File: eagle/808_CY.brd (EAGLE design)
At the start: 100 x 80 mm, 112 parts, among them IC1 TL071P, IC2 TL071P, IC3 TL071P, IC4 TL072P, Q1 2N3904, Q2 2N3904, Q3 2N3904, Q4 2N3904, Q5 2N3904, Q6 2N3904, Q7 2N3904, Q8 2N3906

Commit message: finishing routes manually
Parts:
- R105*: device TR808clone:0207/5V -> TR808clone:0309/10
- R126*: device TR808clone:0207/5V -> TR808clone:0207/7
- moved R126* 13.6 mm to (94.6, 52.1)
- moved R105* 8.03 mm to (81.3, 27.9), turned to 180 degrees
- moved R123* 6.35 mm to (69.8, 25.4), turned to 270 degrees
- moved R127* 2.84 mm to (85.1, 48.3), turned to 180 degrees
- moved R92* 2.84 mm to (67.3, 26.7)
- moved C59* 2.54 mm to (91.4, 47.0), turned to 180 degrees
- moved R85* 2.54 mm to (76.2, 34.3)
- moved R89* 1.27 mm to (64.8, 25.4)
- moved Q6 1.27 mm to (78.7, 24.1)
- moved D6* 1.27 mm to (85.1, 58.4)
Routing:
- net GND: track 0.00 -> 533.4 mm
- net N$558: track 0.00 -> 100.7 mm
- net N$544: track 0.00 -> 84.2 mm
- net +15V: track 0.00 -> 83.7 mm
- net -15V: track 0.00 -> 69.1 mm
- net N$513: track 0.00 -> 63.8 mm
- net N$223: track 0.00 -> 52.2 mm
- net N$546: track 0.00 -> 45.7 mm
- net N$528: track 0.00 -> 41.6 mm
- net TO_HH: track 0.00 -> 36.2 mm
- net N$529: track 0.00 -> 34.9 mm
- net CY: track 0.00 -> 33.1 mm
- net N$508: track 0.00 -> 27.5 mm
- net N$539: track 0.00 -> 26.9 mm
- net TRIG*: track 0.00 -> 26.9 mm
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
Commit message: more routes
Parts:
- C47*: device TR808clone:C035-025X75 -> TR808clone:C050-035X075
- R166*: device TR808clone:0207/5V -> TR808clone:0207/7
- moved R93* 4.02 mm to (54.6, 35.6)
- moved R110* 2.30 mm to (39.1, 32.8)
- moved R113* 1.98 mm to (48.5, 29.2)
- moved R118* 1.83 mm to (32.8, 16.3)
- moved R128* 1.80 mm to (26.7, 10.2), turned to 180 degrees
- moved C11* 1.80 mm to (21.6, 72.4), turned to 270 degrees
- moved R10* 1.78 mm to (57.7, 3.81)
- moved R129* 1.55 mm to (13.0, 39.6), turned to 0 degrees
- moved R166* 1.42 mm to (10.8, 17.8)
- moved C77* 1.27 mm to (22.9, 14.0), turned to 0 degrees
- moved Q6 1.27 mm to (78.7, 22.9)
- moved R88* 1.27 mm to (75.9, 69.3)
- moved R56* 0.80 mm to (39.6, 68.1)
- moved R84* 0.80 mm to (83.6, 22.1)
- moved R114* 0.76 mm to (39.4, 25.9)
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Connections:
- net GND: now also C47*.2; no longer C47*.P$2
- net N$523: now also C47*.1; no longer C47*.P$1
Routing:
- net GND: track 533.4 -> 402.5 mm
- net N$548: track 10.6 -> 109.9 mm
- net N$178: track 5.08 -> 71.0 mm, vias 0 -> 2
- net N$7: track 0.00 -> 9.73 mm
- net N$223: track 52.2 -> 47.3 mm
- net N$529: track 34.9 -> 39.5 mm
- net N$495: track 6.84 -> 2.53 mm
- net N$544: track 84.2 -> 80.7 mm
- net N$515: track 23.0 -> 19.6 mm
- net N$561: track 19.9 -> 17.6 mm
- net N$535: track 14.7 -> 12.4 mm
- net N$549: track 11.1 -> 8.81 mm
- net N$516: track 14.5 -> 12.5 mm
- net N$4: track 5.58 -> 4.09 mm
- net N$533: track 26.1 -> 24.7 mm
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
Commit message: more routes
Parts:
- C55*: device TR808clone:C035-025X75 -> TR808clone:C050-030X075
- R109*, R111*, R91*, R93*: device TR808clone:0207/5V -> TR808clone:0207/7
- moved R91* 32.6 mm to (61.0, 32.3), turned to 180 degrees
- moved R115* 21.3 mm to (42.7, 27.7), turned to 180 degrees
- moved R166* 6.14 mm to (16.4, 15.2)
- moved C77* 5.57 mm to (26.7, 9.91), turned to 270 degrees
- moved D12* 4.93 mm to (70.9, 73.9)
- moved C78* 4.10 mm to (11.2, 18.3), turned to 90 degrees
- moved R128* 3.70 mm to (30.2, 9.14), turned to 270 degrees
- moved C45* 2.84 mm to (76.2, 76.2), turned to 180 degrees
- moved R93* 2.30 mm to (56.9, 35.3)
- moved R106* 1.80 mm to (62.0, 39.9)
- moved R101* 1.63 mm to (48.5, 68.6)
- moved C38* 1.27 mm to (78.5, 62.0)
- moved C56* 1.27 mm to (39.1, 20.8)
- moved C41* 1.27 mm to (58.4, 24.1)
- moved R89* 1.27 mm to (63.5, 25.4)
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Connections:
- net N$533: now also C55*.1; no longer C55*.P$1
- net N$536: now also C55*.2; no longer C55*.P$2
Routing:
- net GND: track 402.5 -> 561.5 mm, vias 0 -> 2
- net +15V: track 82.6 -> 154.4 mm, vias 0 -> 2
- net -15V: track 69.1 -> 123.9 mm
- net N$528: track 41.7 -> 7.98 mm
- net N$558: track 100.7 -> 74.4 mm
- net N$544: track 80.7 -> 68.5 mm
- net N$541: track 16.7 -> 6.91 mm
- net N$508: track 27.5 -> 22.5 mm
- net N$7: track 9.73 -> 5.57 mm
- net N$546: track 46.7 -> 42.9 mm
- net N$507: track 8.23 -> 11.7 mm
- net N$223: track 47.3 -> 44.5 mm
- net N$171: track 15.4 -> 12.6 mm
- net N$561: track 17.6 -> 15.1 mm
- net N$533: track 24.7 -> 22.9 mm
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
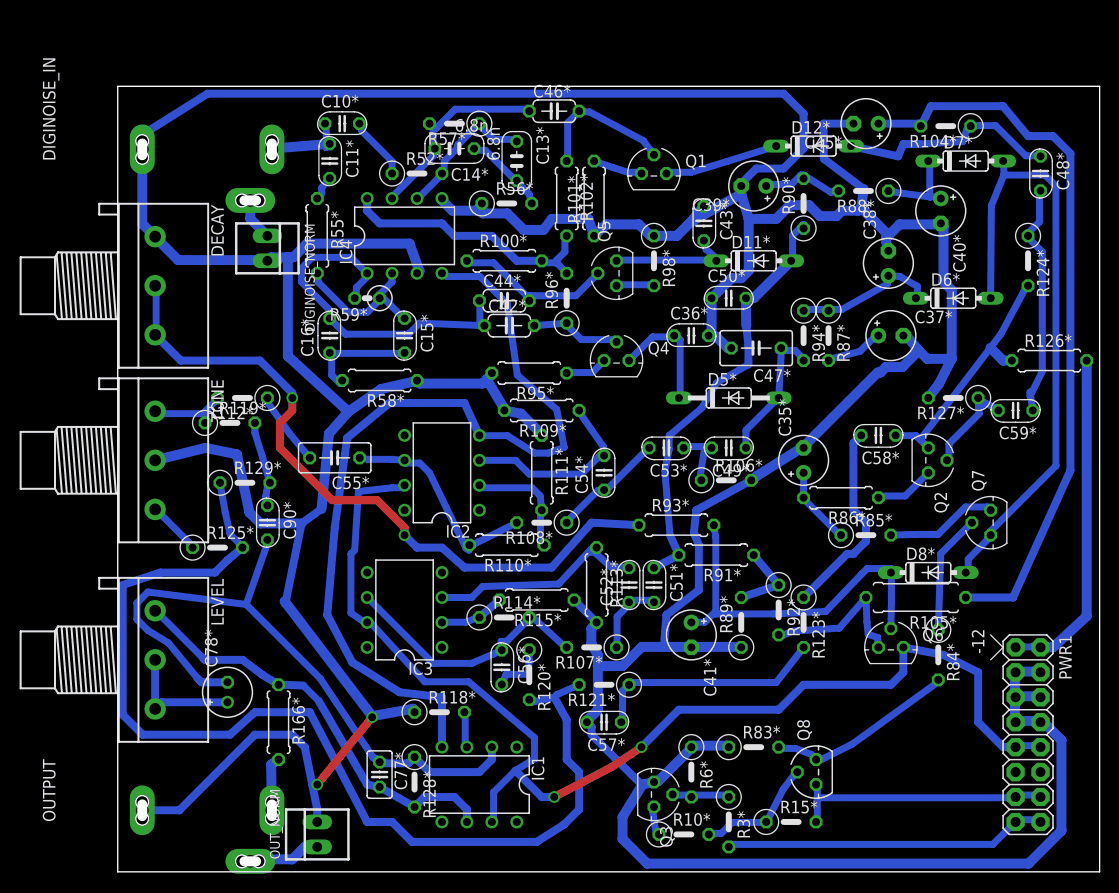
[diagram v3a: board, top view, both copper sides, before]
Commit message: ar 94pct with 072 replacing two 071
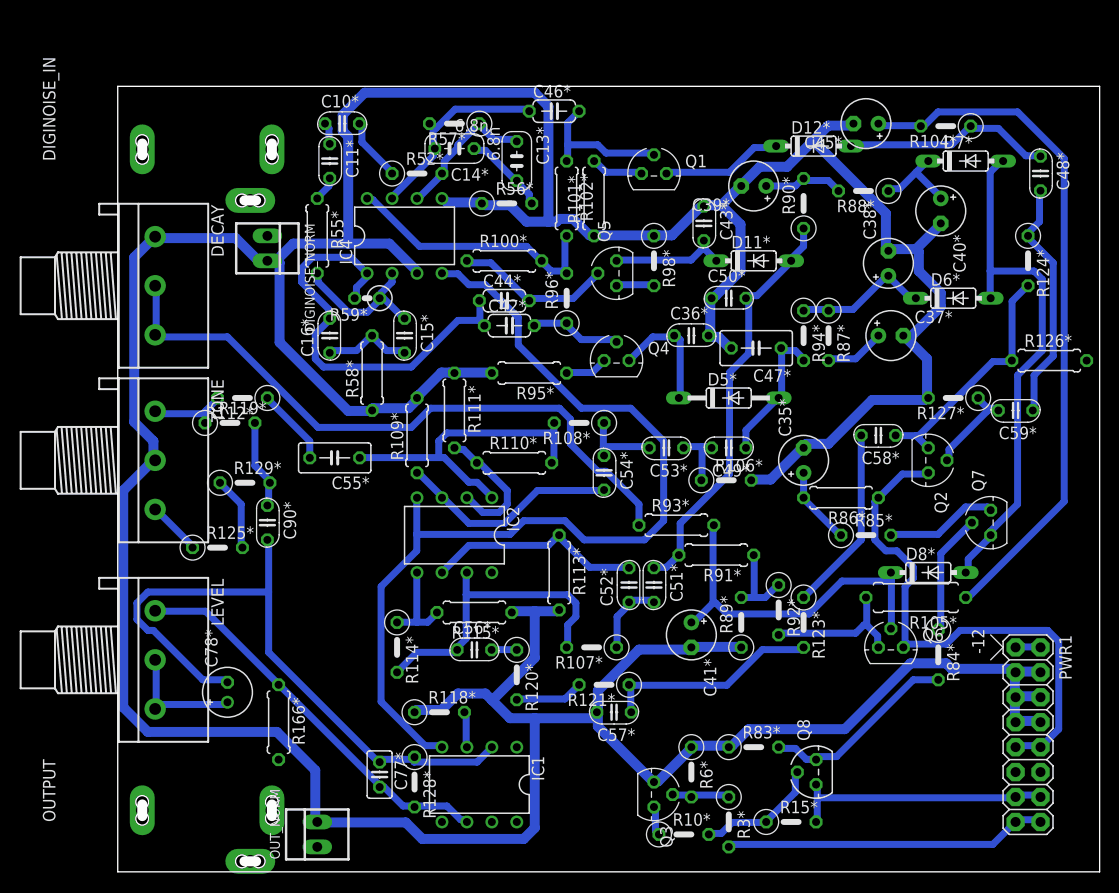
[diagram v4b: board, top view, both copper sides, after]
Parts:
- removed IC3: TL071P, linear:DIL08
- IC2: value TL071P -> TL072P
- moved R109* 13.0 mm to (30.5, 44.5), turned to 90 degrees
- moved R114* 11.3 mm to (28.4, 22.9), turned to 270 degrees
- moved R111* 10.9 mm to (34.3, 47.0)
- moved R108* 10.9 mm to (47.0, 45.7)
- moved R110* 8.42 mm to (40.4, 41.7), turned to 0 degrees
- moved IC2 6.48 mm to (34.3, 34.3), turned to 180 degrees
- moved R115* 6.48 mm to (36.3, 26.4)
- moved R113* 4.02 mm to (45.0, 30.5)
- moved C56* 3.31 mm to (36.3, 22.6), turned to 0 degrees
- moved C57* 1.44 mm to (50.5, 16.3)
- moved R120* 1.27 mm to (40.6, 20.1)
- moved R58* 1.08 mm to (25.9, 50.8), turned to 90 degrees
- turned C54* to 270 degrees
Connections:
- net +15V: now also IC2.8; no longer IC2.7, IC3.7
- net -15V: no longer IC3.4
- net N$533: now also IC2.1; no longer IC2.6
- net N$538: now also IC2.6; no longer IC3.3
- net N$539: now also IC2.7; no longer IC3.6
- net N$541: now also IC2.5; no longer IC3.2
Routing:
- net N$548: track 108.6 -> 14.5 mm
- net GND: track 561.5 -> 475.2 mm, vias 2 -> 0
- net +15V: track 154.4 -> 82.9 mm, vias 2 -> 0
- net -15V: track 123.9 -> 99.7 mm
- net N$533: track 22.9 -> 33.1 mm
- net N$513: track 63.8 -> 53.9 mm
- net N$5: track 7.43 -> 0.00 mm
- net LT_LC_OUT1: track 8.94 -> 2.23 mm
- net TO_HH: track 37.3 -> 43.7 mm
- net N$7: track 5.57 -> 0.00 mm
- net N$178: track 71.7 -> 66.8 mm, vias 2 -> 0
- net N$539: track 26.9 -> 31.8 mm
- net N$6: track 4.33 -> 0.00 mm
- net N$558: track 74.4 -> 70.6 mm
- net N$534: track 11.6 -> 8.09 mm
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
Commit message: finishing manually with two 072
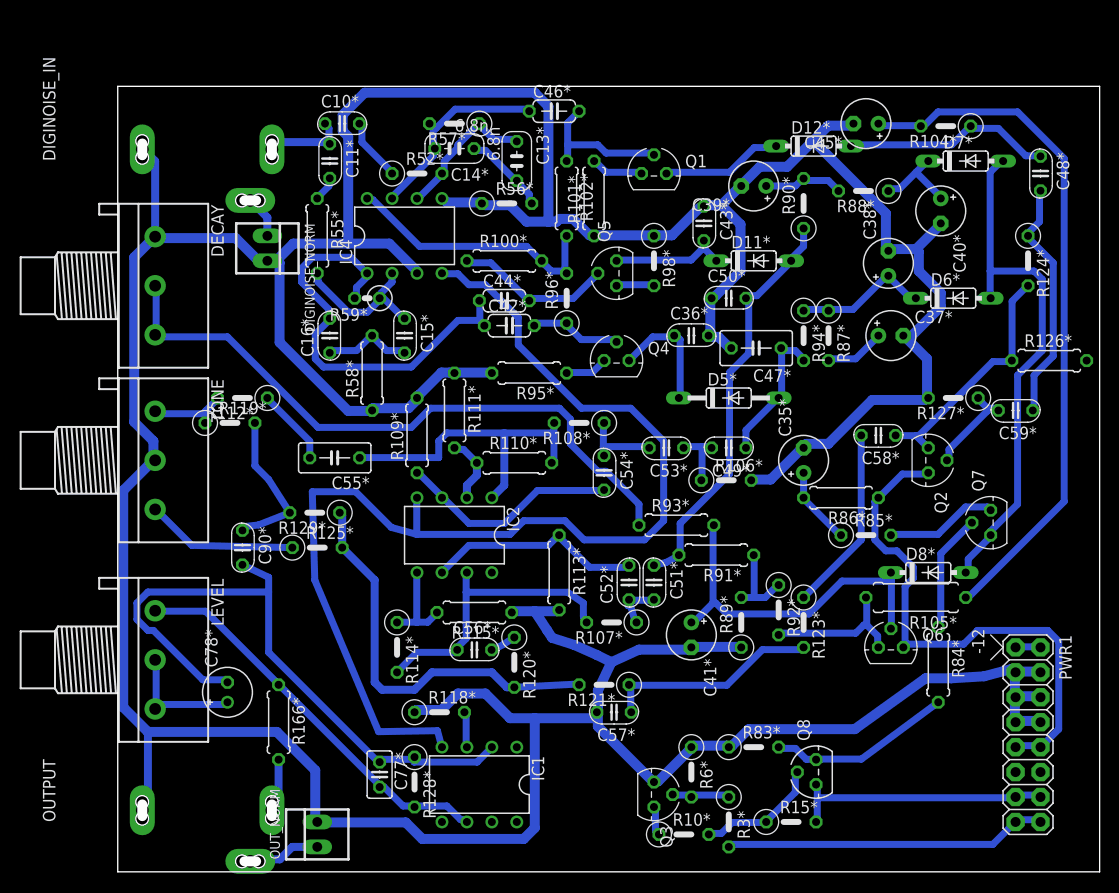
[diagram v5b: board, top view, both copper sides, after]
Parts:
- R84*: device TR808clone:0207/5V -> TR808clone:0207/7
- moved R125* 10.2 mm to (20.3, 33.0)
- moved R129* 7.74 mm to (20.1, 36.6), turned to 180 degrees
- moved C90* 3.59 mm to (12.7, 33.0)
- moved R107* 3.25 mm to (50.3, 25.4)
- moved R120* 1.30 mm to (40.4, 21.3)
- moved R84* 1.02 mm to (83.6, 21.1)
- moved C51* 0.25 mm to (54.6, 29.5)
- moved C52* 0.25 mm to (52.1, 29.5)
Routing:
- net N$548: track 14.5 -> 41.4 mm
- net -15V: track 99.7 -> 118.8 mm
- net GND: track 475.2 -> 491.1 mm
- net N$537: track 5.48 -> 15.5 mm
- net N$5: track 0.00 -> 7.43 mm
- net N$535: track 13.7 -> 6.93 mm
- net N$549: track 9.10 -> 15.7 mm
- net LT_LC_OUT1: track 2.23 -> 8.35 mm
- net N$7: track 0.00 -> 5.44 mm
- net N$6: track 0.00 -> 4.33 mm
- net N$540: track 7.84 -> 5.85 mm
- net N$539: track 31.8 -> 30.1 mm
- net N$515: track 20.3 -> 18.7 mm
- net N$544: track 68.1 -> 67.1 mm

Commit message: more manual routes
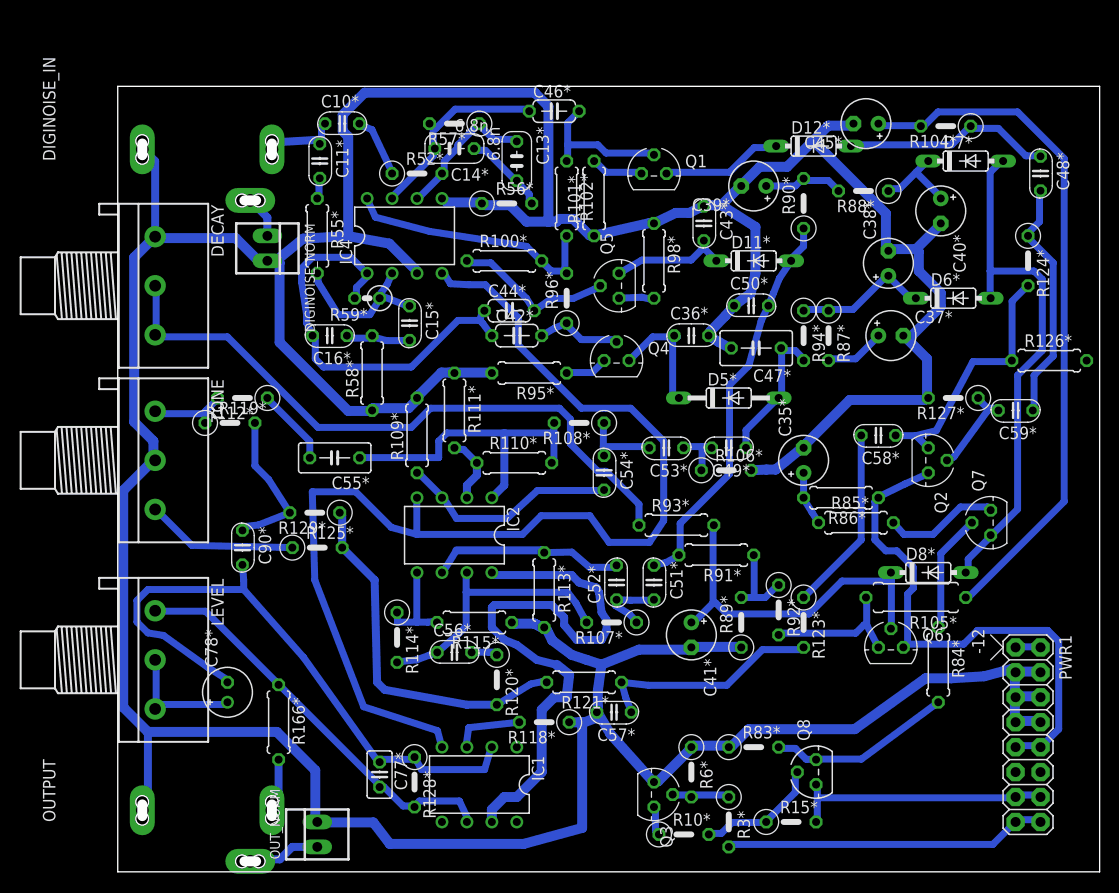
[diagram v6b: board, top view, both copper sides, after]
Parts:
- R121*, R85*, R98*: device TR808clone:0207/5V -> TR808clone:0207/7
- moved R118* 10.7 mm to (43.4, 15.2), turned to 180 degrees
- moved R120* 2.51 mm to (38.6, 19.6)
- moved C50* 2.41 mm to (64.5, 57.7)
- moved R113* 2.34 mm to (43.4, 28.7)
- moved C56* 2.05 mm to (34.3, 22.4)
- moved R121* 2.05 mm to (47.5, 19.3)
- moved R85* 1.63 mm to (75.2, 35.6)
- moved C15* 1.37 mm to (29.7, 55.9)
- moved Q5 1.30 mm to (51.1, 59.7)
- moved C52* 1.27 mm to (50.8, 29.5)
- moved C42* 1.27 mm to (40.6, 54.6)
- moved C44* 1.14 mm to (39.9, 57.1)
- moved R114* 1.02 mm to (28.4, 23.9)
- moved R115* 1.02 mm to (36.3, 25.4)
- moved C11* 1.02 mm to (20.6, 72.4)
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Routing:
- net +15V: track 82.9 -> 143.2 mm
- net GND: track 491.1 -> 475.1 mm
- net N$548: track 41.4 -> 37.1 mm
- net N$4: track 3.71 -> 7.20 mm
- net N$544: track 67.1 -> 64.1 mm
- net N$511: track 7.97 -> 5.52 mm
- net N$538: track 22.2 -> 19.8 mm
- net N$539: track 30.1 -> 28.1 mm
- net N$556: track 9.11 -> 7.12 mm
- net N$223: track 42.5 -> 40.6 mm
- net N$540: track 5.85 -> 7.21 mm
- net N$546: track 41.1 -> 42.4 mm
- net N$177: track 25.1 -> 26.2 mm
- net N$554: track 22.4 -> 23.5 mm
- net N$530: track 6.40 -> 5.38 mm
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
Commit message: routed and tweaked
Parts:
- C41*: device TR808clone:E2,5-5 -> TR808clone:E3,5-8
- R123*, R89*, R92*: device TR808clone:0207/5V -> TR808clone:0207/7
- moved R126* 19.0 mm to (76.6, 47.0), turned to 180 degrees
- moved R124* 9.94 mm to (87.4, 53.8), turned to 180 degrees
- moved D7* 7.38 mm to (85.9, 65.0), turned to 270 degrees
- moved C48* 7.03 mm to (88.6, 66.5)
- moved R104* 4.02 mm to (82.0, 72.6), turned to 90 degrees
- moved C59* 3.31 mm to (88.1, 46.7)
- moved R119* 3.30 mm to (12.7, 42.7), turned to 270 degrees
- moved C40* 2.87 mm to (81.8, 65.3)
- moved R90* 2.75 mm to (71.4, 65.8)
- moved C58* 2.54 mm to (77.5, 41.9)
- moved R127* 2.54 mm to (83.1, 49.8)
- moved R56* 2.50 mm to (37.3, 69.1), turned to 90 degrees
- moved R87* 2.27 mm to (73.4, 56.6)
- moved C45* 2.03 mm to (78.2, 76.2)
- moved D6* 2.03 mm to (83.1, 58.4)
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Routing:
- net +15V: track 143.2 -> 240.1 mm, vias 0 -> 2
- net -15V: track 119.0 -> 200.7 mm, vias 0 -> 2
- net N$513: track 54.2 -> 35.4 mm
- net GND: track 475.1 -> 487.1 mm
- net N$558: track 70.6 -> 59.7 mm
- net N$550: track 24.8 -> 18.2 mm
- net N$527: track 14.9 -> 19.6 mm
- net N$177: track 26.2 -> 21.6 mm
- net N$549: track 15.7 -> 11.5 mm
- net N$553: track 18.9 -> 15.2 mm
- net N$508: track 21.6 -> 18.5 mm
- net N$532: track 8.34 -> 11.5 mm
- net N$561: track 14.3 -> 11.4 mm
- net N$547: track 3.00 -> 5.19 mm
- net N$512: track 11.7 -> 9.69 mm
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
